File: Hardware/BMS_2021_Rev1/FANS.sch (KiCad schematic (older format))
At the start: 5 parts

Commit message: buzzer started, 5v buck needs R values
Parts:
- removed C?: C, symbol Device:C
- removed R? (x2): R, symbol Device:R
- removed R?: R_Shunt, symbol Device:R_Shunt
- removed U?: INA226, Package_SO:VSSOP-10_3x3mm_P0.5mm, symbol Analog_ADC:INA226
- added Conn?: Molex_SL_08, symbol MRDT_Connectors:Molex_SL_08
- added Q?: Q_NMOS_DGS, symbol Device:Q_NMOS_DGS
- added R?: 10kΩ, symbol Device:R
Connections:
- net labels added: fan_control
- net labels removed: I2C_Interface(?), PV, V_in
- wire segments 38 -> 21
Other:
- note removed: "Doucmentation says connect VBUS to power supply rail, does this work\n"
- note removed: "Where should PV and ground go?\n"

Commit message: done (need to do LEDs)
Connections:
- net +5V renamed 5V
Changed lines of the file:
@@
 $Descr A 11000 8500
 encoding utf-8
-Sheet 10 10
+Sheet 7 11
 Title ""
 Date ""
@@
 Wire Wire Line
 	2300 2000 2400 2000
-$Comp
-L power:+5V #PWR?
-U 1 1 5F873378
-P 2400 2000
-F 0 "#PWR?" H 2400 1850 50  0001 C CNN
-F 1 "+5V" V 2415 2128 50  0000 L CNN
-F 2 "" H 2400 2000 50  0001 C CNN
-F 3 "" H 2400 2000 50  0001 C CNN
-	1    2400 2000
-	0    1    1    0
-$EndComp
 Wire Wire Line
 	2300 2200 2400 2200
-$Comp
-L power:+5V #PWR?
-U 1 1 5F873113
-P 2400 2200
-F 0 "#PWR?" H 2400 2050 50  0001 C CNN
-F 1 "+5V" V 2415 2328 50  0000 L CNN
-F 2 "" H 2400 2200 50  0001 C CNN
-F 3 "" H 2400 2200 50  0001 C CNN
-	1    2400 2200
-	0    1    1    0
-$EndComp
 Wire Wire Line
 	2300 2400 2400 2400
-$Comp
-L power:+5V #PWR?
-U 1 1 5F873044
-P 2400 2400
-F 0 "#PWR?" H 2400 2250 50  0001 C CNN
-F 1 "+5V" V 2415 2528 50  0000 L CNN
-F 2 "" H 2400 2400 50  0001 C CNN
-F 3 "" H 2400 2400 50  0001 C CNN
-	1    2400 2400
-	0    1    1    0
-$EndComp
 Wire Wire Line
 	2300 2600 2400 2600
-$Comp
-L power:+5V #PWR?
-U 1 1 5F872133
-P 2400 2600
-F 0 "#PWR?" H 2400 2450 50  0001 C CNN
-F 1 "+5V" V 2415 2728 50  0000 L CNN
-F 2 "" H 2400 2600 50  0001 C CNN
-F 3 "" H 2400 2600 50  0001 C CNN
-	1    2400 2600
-	0    1    1    0
-$EndComp
 Wire Wire Line
 	2300 2100 3050 2100
@@
 	-1   0    0    1
 $EndComp
+Text HLabel 2400 2000 2    50   Input ~ 0
+5V
+Text HLabel 2400 2200 2    50   Input ~ 0
+5V
+Text HLabel 2400 2400 2    50   Input ~ 0
+5V
+Text HLabel 2400 2600 2    50   Input ~ 0
+5V
 $EndSCHEMATC

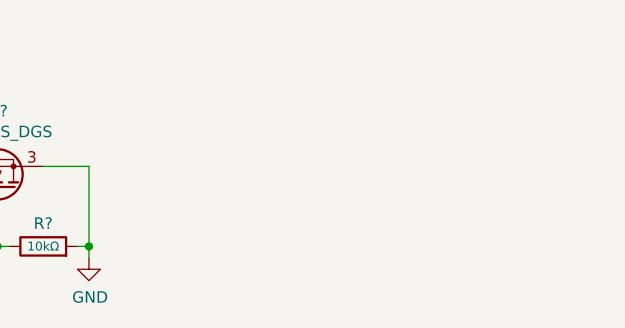
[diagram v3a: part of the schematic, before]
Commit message: notes from PDR made. to be fixed
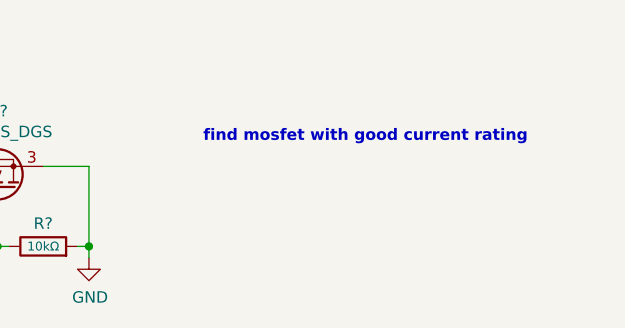
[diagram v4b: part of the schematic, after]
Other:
- note added: "find mosfet with good current rating\n"
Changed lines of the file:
@@
 $Descr A 11000 8500
 encoding utf-8
-Sheet 7 11
+Sheet 6 11
 Title ""
 Date ""
@@
 Text HLabel 2400 2600 2    50   Input ~ 0
 5V
+Text Notes 4550 2250 0    50   ~ 10
+find mosfet with good current rating\n
 $EndSCHEMATC

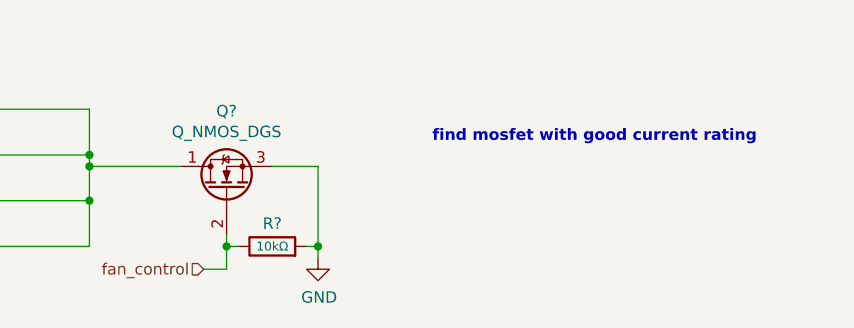
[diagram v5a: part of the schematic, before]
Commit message: added libraries to docs folder
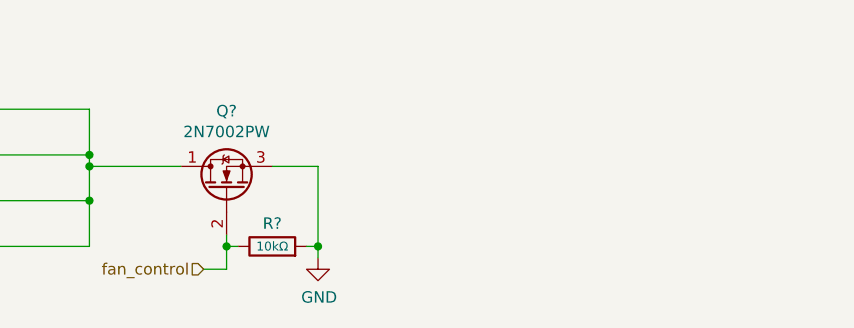
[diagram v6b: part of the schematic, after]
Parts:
- Q?: value Q_NMOS_DGS -> 2N7002PW
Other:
- note removed: "find mosfet with good current rating\n"
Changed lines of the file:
@@
 P 3650 2450
 F 0 "Q?" V 3992 2450 50  0000 C CNN
-F 1 "Q_NMOS_DGS" V 3901 2450 50  0000 C CNN
+F 1 "2N7002PW" V 3901 2450 50  0000 C CNN
 F 2 "" H 3850 2550 50  0001 C CNN
-F 3 "~" H 3650 2450 50  0001 C CNN
+F 3 "https://www.digikey.com/en/products/detail/nexperia-usa-inc/2N7002PW-115/2531274" H 3650 2450 50  0001 C CNN
 	1    3650 2450
 	0    -1   -1   0
@@
 Text HLabel 2400 2600 2    50   Input ~ 0
 5V
-Text Notes 4550 2250 0    50   ~ 10
-find mosfet with good current rating\n
 $EndSCHEMATC

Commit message: annotated sch.
some ICs got moved around- solve later
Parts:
- gave numbers to parts that had none: 3
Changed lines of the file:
@@
 $EndDescr
 $Comp
-L Device:Q_NMOS_DGS Q?
+L Device:Q_NMOS_DGS Q1
 U 1 1 5F87380D
 P 3650 2450
-F 0 "Q?" V 3992 2450 50  0000 C CNN
+F 0 "Q1" V 3992 2450 50  0000 C CNN
 F 1 "2N7002PW" V 3901 2450 50  0000 C CNN
 F 2 "" H 3850 2550 50  0001 C CNN
@@
 fan_control
 $Comp
-L power:GND #PWR?
+L power:GND #PWR044
 U 1 1 5F8763F8
 P 4050 2750
-F 0 "#PWR?" H 4050 2500 50  0001 C CNN
+F 0 "#PWR044" H 4050 2500 50  0001 C CNN
 F 1 "GND" H 4055 2577 50  0000 C CNN
 F 2 "" H 4050 2750 50  0001 C CNN
@@
 $EndComp
 $Comp
-L Device:R R?
+L Device:R R36
 U 1 1 5F876804
 P 3850 2700
-F 0 "R?" V 3950 2700 50  0000 C CNN
+F 0 "R36" V 3950 2700 50  0000 C CNN
 F 1 "10kΩ" V 3850 2700 39  0000 C CNN
 F 2 "" V 3780 2700 50  0001 C CNN
@@
 	2300 2700 3050 2700
 $Comp
-L MRDT_Connectors:Molex_SL_08 Conn?
+L MRDT_Connectors:Molex_SL_08 Conn4
 U 1 1 5F863577
 P 2100 1950
-F 0 "Conn?" H 2042 1763 60  0000 C CNN
+F 0 "Conn4" H 2042 1763 60  0000 C CNN
 F 1 "Molex_SL_08" H 2042 1869 60  0000 C CNN
 F 2 "" H 2100 2250 60  0001 C CNN

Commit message: Began assigning footprints
Downloaded some footprint files from UltraLibrarian. Put in BMS_Hardware>Documentation> then copied files where they need to go
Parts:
- Conn4: footprint (none) -> MRDT_Connectors:MOLEX_SL_08_Vertical
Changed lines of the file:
@@
 F 0 "Conn4" H 2042 1763 60  0000 C CNN
 F 1 "Molex_SL_08" H 2042 1869 60  0000 C CNN
-F 2 "" H 2100 2250 60  0001 C CNN
+F 2 "MRDT_Connectors:MOLEX_SL_08_Vertical" H 2100 2250 60  0001 C CNN
 F 3 "" H 2100 2250 60  0001 C CNN
 	1    2100 1950
